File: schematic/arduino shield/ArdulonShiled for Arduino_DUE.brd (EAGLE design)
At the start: 101.6 x 53.3 mm, 25 parts, among them X1 5566-14, X2 5566-14, X3 5566-14

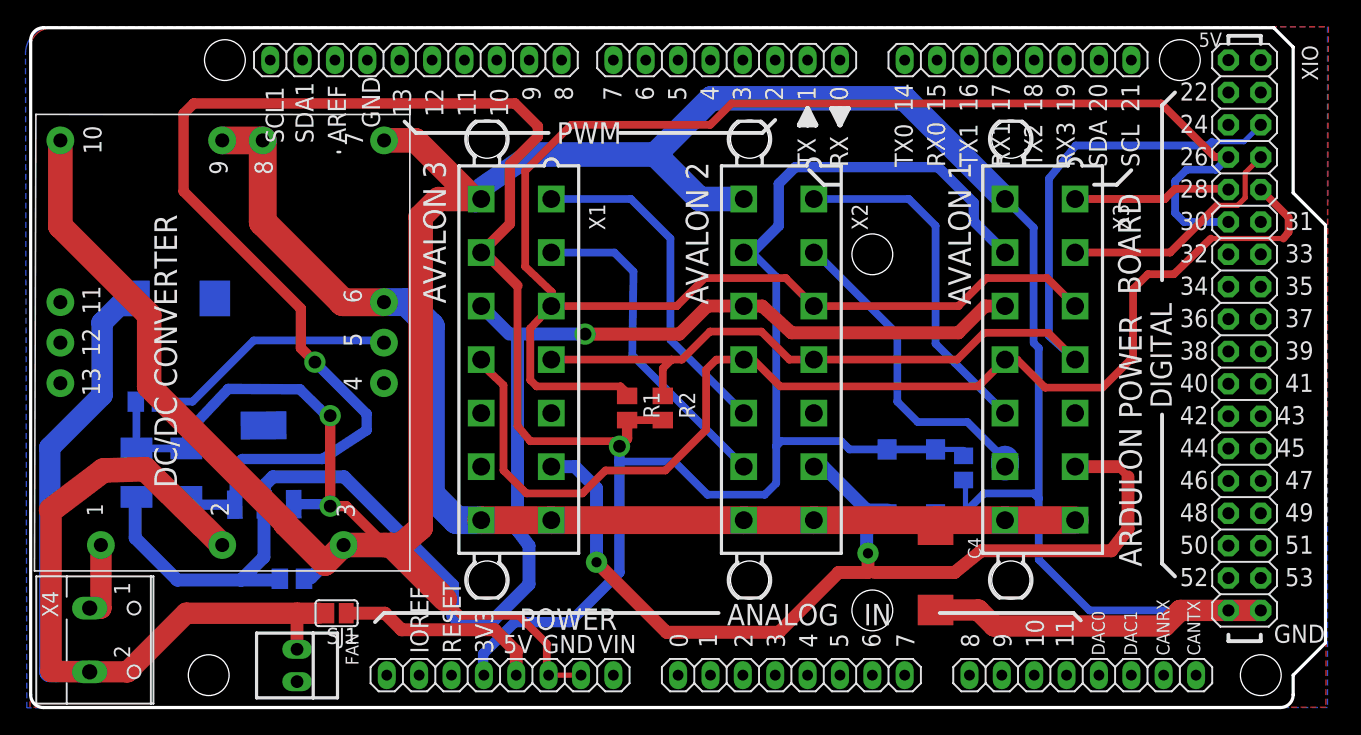
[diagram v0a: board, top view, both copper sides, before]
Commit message: added some datasheets, updated schematic
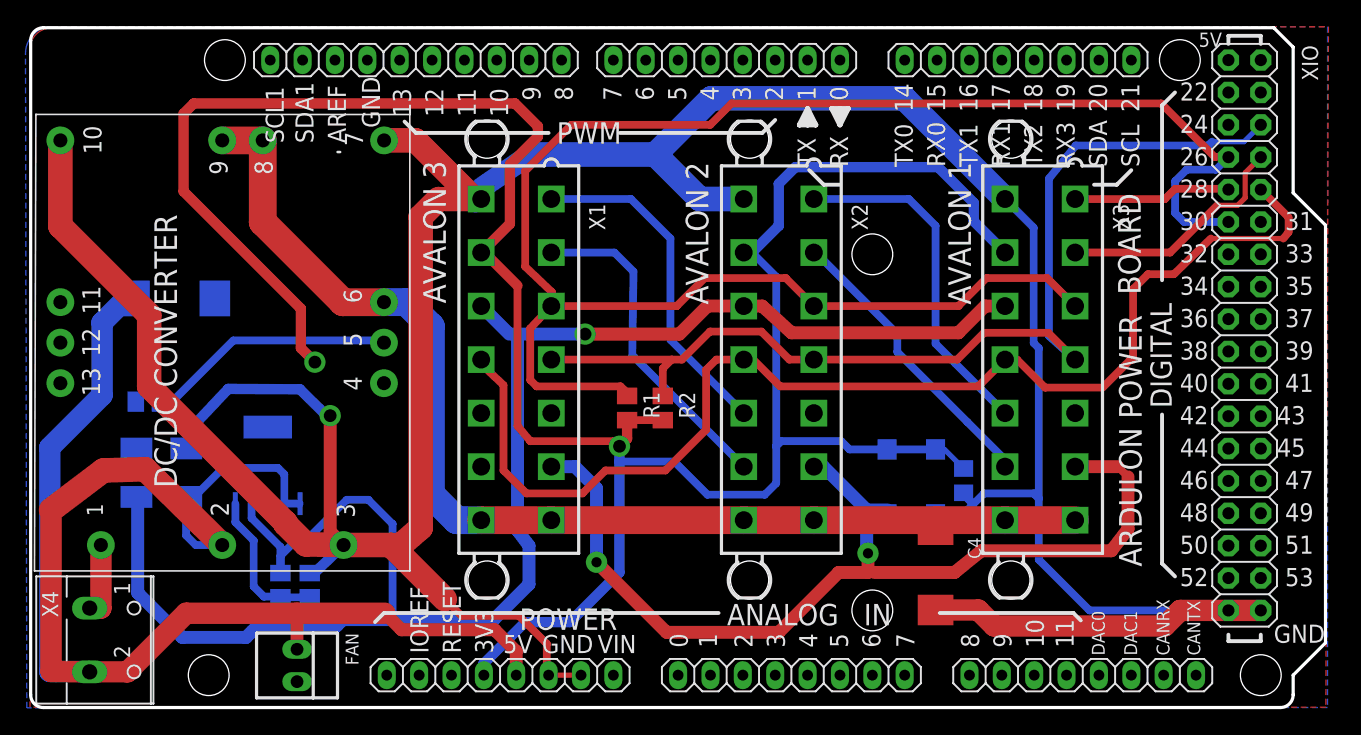
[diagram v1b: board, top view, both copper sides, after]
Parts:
- removed IC1: (no value), SparkFun:SOT223
- removed SJ1: (no value), jumper:SJ
- added R5: (no value), rcl:M0805
- added U$2: MCP1824T, BaseApp:SOT223-5
- R4: value 120 -> 20K
- moved R4 1.49 mm to (21.9, 9.60), turned to 270 degrees
- moved C5 1.00 mm to (73.2, 17.8)
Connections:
- net VCC12 renamed VCC0.9
- removed net VCC12REF: C2.A, IC1.2, R4.2, X1.10, X2.10, X3.10
- new net VCC1REF: C2.A, R5.1, U$2.4, X1.10, X2.10, X3.10
- net GND: now also U$2.3, U$2.TAB; no longer IC1.1
- net N$1: now also R4.2, R5.2, U$2.N; no longer POWER.5, SJ1.1
- net VCC: no longer C1.A, IC1.3
- net VCC5V: now also C1.A, POWER.5, U$2.1, U$2.2; no longer SJ1.2
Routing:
- net VCC1REF: track 0.00 -> 133.0 mm, vias 0 -> 1
- net VCC12REF: track 118.3 -> 0.00 mm, vias 1 -> 0
- net VCC5V: track 91.5 -> 128.6 mm
- net VCC: track 221.0 -> 194.8 mm
- net GND: track 303.4 -> 284.7 mm, vias 2 -> 1
- net N$1: track 17.0 -> 11.8 mm
- net N$4: track 25.6 -> 23.3 mm
